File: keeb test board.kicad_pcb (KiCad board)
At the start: 2 copper layers, 61 x 103.8 mm, 62 parts, among them SW1 SW_Push, SW10 SW_Push, SW11 SW_Push, SW12 SW_Push, SW13 SW_Push, SW14 SW_Push, SW15 SW_Push, SW2 SW_Push, SW3 SW_Push, SW4 SW_Push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

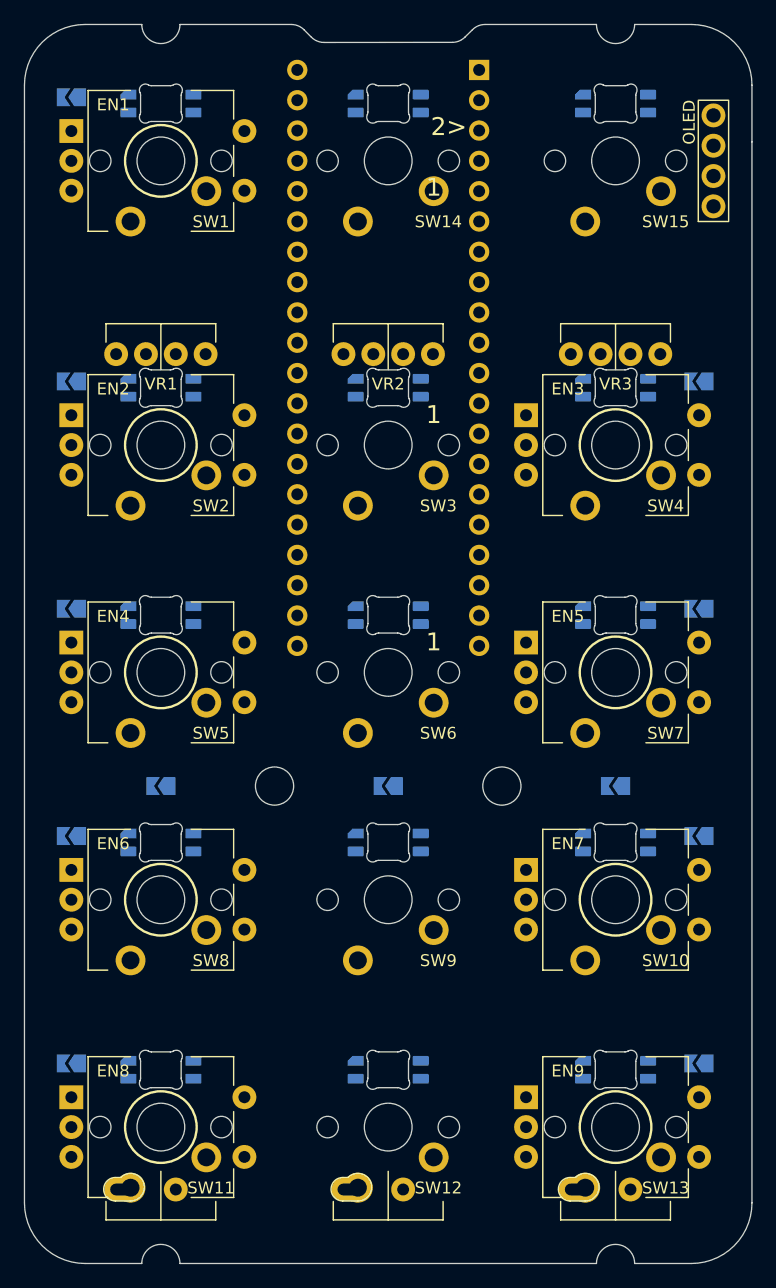
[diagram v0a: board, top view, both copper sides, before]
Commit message: initial board routing
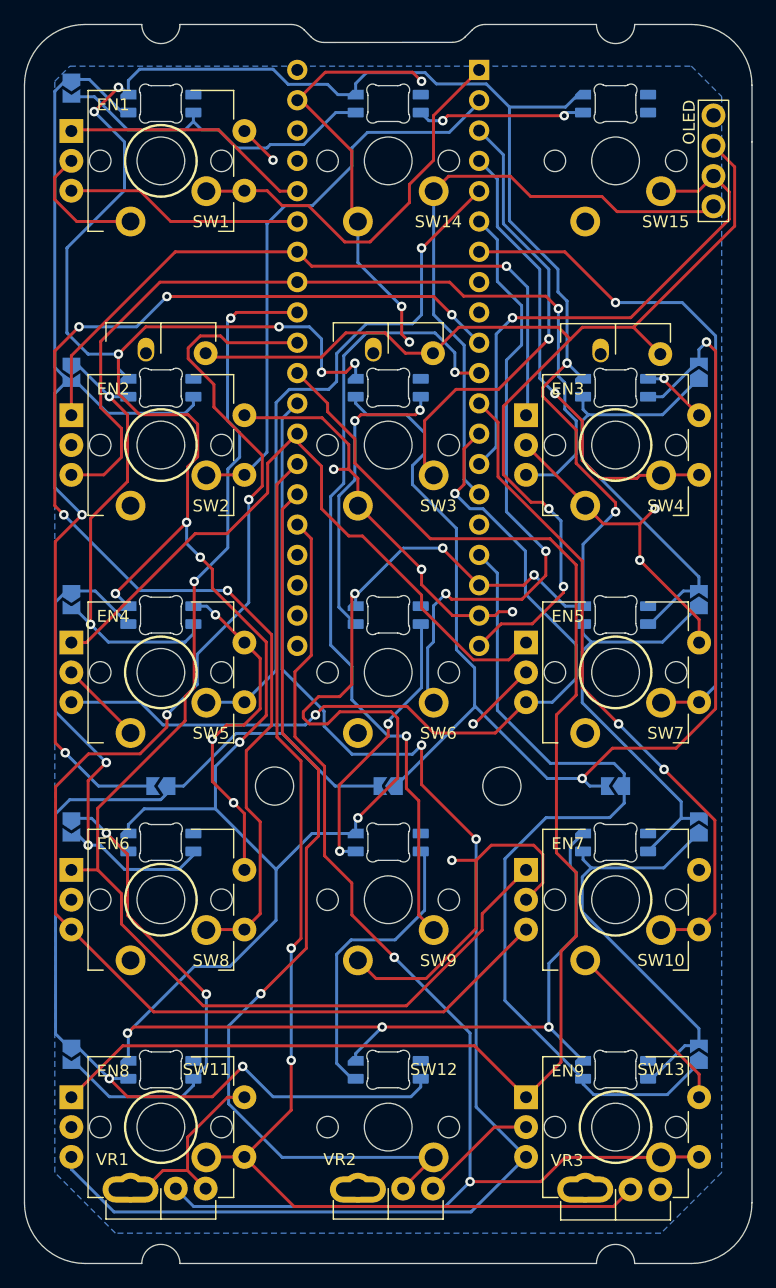
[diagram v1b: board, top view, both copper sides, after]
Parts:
- moved VR3 70.0 mm to (111.2, 152.8), turned to 180 degrees
- moved VR1 69.9 mm to (73.1, 152.7), turned to 180 degrees
- moved VR2 69.9 mm to (92.2, 152.7), turned to 180 degrees
- moved JP1 0.76 mm to (118.2, 141.5), turned to 90 degrees
- moved JP10 0.76 mm to (65.6, 122.4), turned to -90 degrees
- moved JP11 0.76 mm to (65.6, 103.4), turned to -90 degrees
- moved JP12 0.76 mm to (65.6, 84.3), turned to -90 degrees
- moved JP13 0.76 mm to (65.6, 60.5), turned to -90 degrees
- moved JP2 0.76 mm to (118.2, 122.4), turned to 90 degrees
- moved JP3 0.76 mm to (118.2, 103.4), turned to 90 degrees
- moved JP4 0.76 mm to (118.2, 84.3), turned to 90 degrees
- moved JP9 0.76 mm to (65.6, 141.5), turned to -90 degrees
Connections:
- EN3 pad A: ENC3A -> ENC2A
- EN3 pad B: ENC3B -> ENC2B
- EN4 pad A: ENC4A -> ENC3A
- EN4 pad B: ENC4B -> ENC3B
- EN5 pad A: ENC4A -> ENC3A
- EN5 pad B: ENC4B -> ENC3B
- EN6 pad A: ENC5A -> ENC4A
- EN6 pad B: ENC5B -> ENC4B
- EN7 pad A: ENC5A -> ENC4A
- EN7 pad B: ENC5B -> ENC4B
- EN8 pad A: ENC6A -> ENC5A
- EN8 pad B: ENC6B -> ENC5B
- EN9 pad A: ENC6A -> ENC5A
- EN9 pad B: ENC6B -> ENC5B
- U1 pad 13: ENC6A -> ENC3B
- U1 pad 28: ENC5B -> ENC3A
- U1 pad 29: ENC5A -> ENC5B
- U1 pad 30: ENC4B -> ENC5A
- U1 pad 31: ENC4A -> ENC4B
- U1 pad 32: ENC2B -> ENC4A
- U1 pad 33: ENC2A -> ENC2B
- U1 pad 34: ENC3B -> ENC2A
- U1 pad 35: ENC3A -> ENC1B
- U1 pad 36: ENC6B -> ENC1A
- U1 pad 38: +3V3 -> unconnected-(U1-Pad38)
- VR1 pad 1B: unconnected-(VR1-Pad1B) -> GND
- VR1 pad 2B: unconnected-(VR1-Pad2B) -> KEY13-POT3
- VR1 pad 3: GND -> unconnected-(VR1-Pad3)
- VR2 pad 1B: unconnected-(VR2-Pad1B) -> GND
- VR2 pad 2B: unconnected-(VR2-Pad2B) -> KEY12-POT2
- VR2 pad 3: GND -> unconnected-(VR2-Pad3)
- VR3 pad 1B: unconnected-(VR3-Pad1B) -> GND
- VR3 pad 2B: unconnected-(VR3-Pad2B) -> KEY11-POT1
- VR3 pad 3: GND -> unconnected-(VR3-Pad3)
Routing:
- net +5V: track 0.00 -> 375.9 mm, vias 0 -> 19
- net GND: track 0.00 -> 231.2 mm, vias 0 -> 15
- net ENC5A: track 0.00 -> 121.0 mm
- net ENC5B: track 0.00 -> 119.2 mm, vias 0 -> 2
- net ENC4B: track 0.00 -> 115.2 mm, vias 0 -> 2
- net KEY13-POT3: track 0.00 -> 108.4 mm, vias 0 -> 2
- net Net-(D4-Pad1): track 0.00 -> 108.2 mm, vias 0 -> 2
- net ENC4A: track 0.00 -> 107.3 mm, vias 0 -> 2
- net KEY8: track 0.00 -> 104.5 mm, vias 0 -> 5
- net KEY11-POT1: track 0.00 -> 99.4 mm, vias 0 -> 2
- net +3V3: track 0.00 -> 97.0 mm, vias 0 -> 2
- net Net-(D8-Pad1): track 0.00 -> 88.0 mm, vias 0 -> 2
- net Net-(D12-Pad1): track 0.00 -> 87.4 mm, vias 0 -> 2
- net KEY12-POT2: track 0.00 -> 78.7 mm, vias 0 -> 1
- net ENC2B: track 0.00 -> 74.3 mm, vias 0 -> 1
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- added copper zone on B.Cu, net GND
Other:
- board text removed: "1"
- board text removed: "2>"

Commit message: routing improvements
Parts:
- moved JP13 0.44 mm to (65.6, 60.9)
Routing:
- net +5V: track 375.9 -> 338.7 mm, vias 19 -> 14
- net GND: track 231.2 -> 254.8 mm, vias 15 -> 13
- net Net-(D7-Pad1): track 25.2 -> 31.0 mm
- net KEY12-POT2: track 78.7 -> 73.7 mm
- net SCL-SW: track 44.1 -> 47.7 mm
- net Net-(D4-Pad1): track 108.2 -> 111.7 mm
- net KEY7: track 57.2 -> 60.6 mm
- net KEY8: track 104.5 -> 107.9 mm
- net ENC5B: track 119.2 -> 116.7 mm
- net Net-(D10-Pad3): track 42.8 -> 45.0 mm
- net KEY10: track 56.0 -> 58.3 mm, vias 2 -> 0
- net LED_DATA: track 73.6 -> 75.7 mm
- net Net-(D5-Pad1): track 25.2 -> 27.0 mm
- net KEY9: track 67.5 -> 69.3 mm
- net KEY6: track 52.4 -> 50.8 mm
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
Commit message: F.silk and via refinement
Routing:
- net GND: track 254.8 -> 258.7 mm, vias 13 -> 14
- net ENC5A: track 121.8 -> 120.2 mm
- net KEY12-POT2: track 73.7 -> 72.2 mm
- net +5V: track 338.7 -> 337.4 mm
- net KEY5: track 58.9 -> 58.3 mm
- net +3V3: track 97.0 -> 96.4 mm

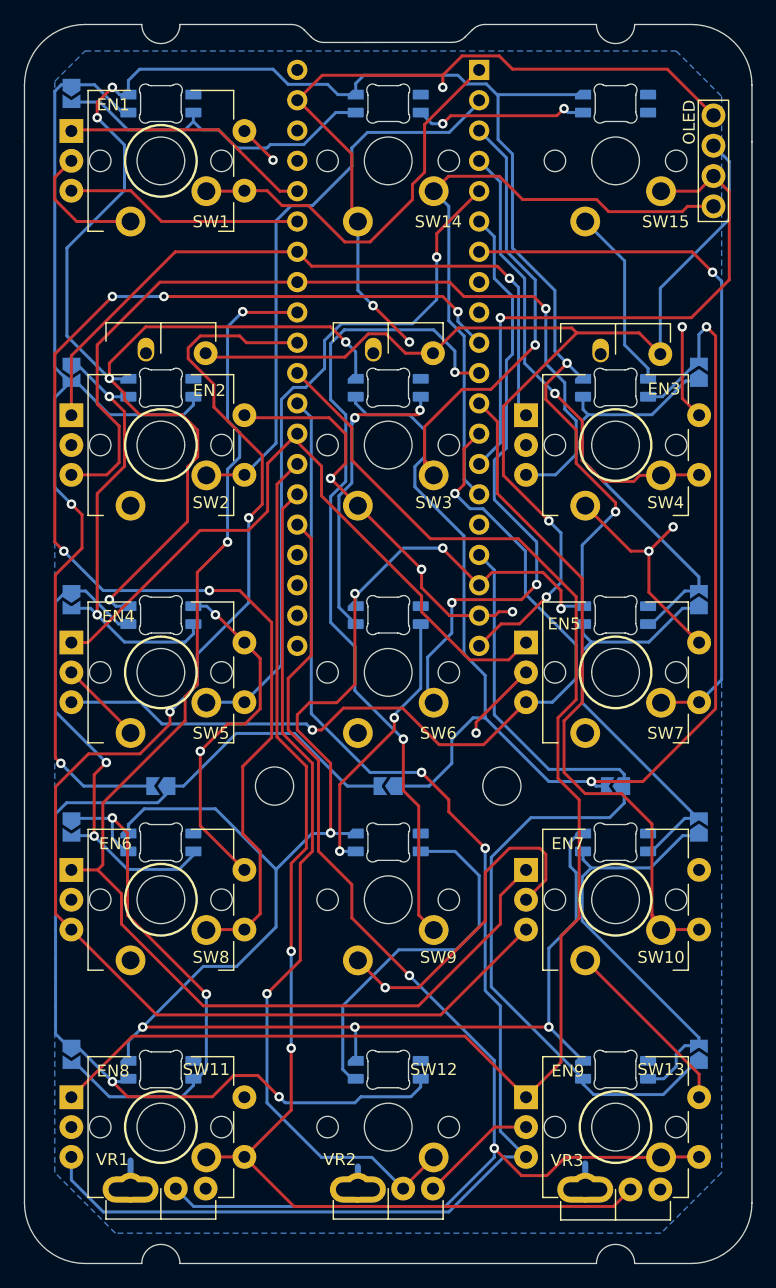
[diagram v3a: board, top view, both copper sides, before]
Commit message: update silks and add copper
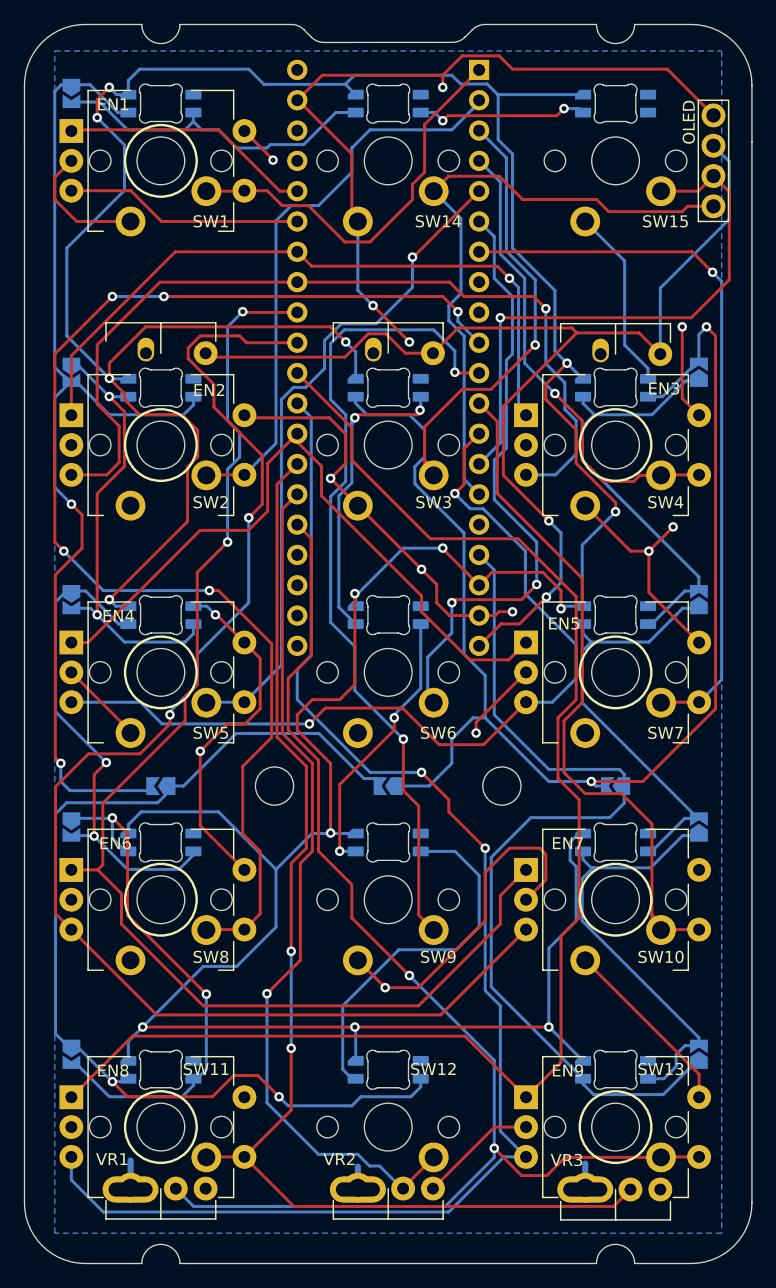
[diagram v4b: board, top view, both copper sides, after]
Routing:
- net KEY5: track 58.3 -> 56.5 mm
- net Net-(D12-Pad1): track 87.7 -> 88.9 mm
- net KEY8: track 107.5 -> 106.4 mm
- net ENC5B: track 116.7 -> 117.6 mm
- net SDA-SW: track 52.4 -> 53.2 mm
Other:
- board text added: "Blue Pill"
